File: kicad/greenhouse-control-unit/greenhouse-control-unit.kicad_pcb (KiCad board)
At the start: 2 copper layers, 55 parts, among them J1 Screw_Terminal_01x02, J10 Conn_01x15_Female, J10_LittleBuck1 Conn_01x01_Female, J11 Conn_01x02_Male, J11_LittleBuck1 Conn_01x01_Female, J12 Screw_Terminal_01x16, J12_BigBuck1 Conn_01x01_Female, J13 Conn_01x10_Female, J13_BigBuck1 Conn_01x01_Female, J14_LittleBuck1 Conn_01x01_Female, J15_LittleBuck1 Conn_01x01_Female, J2 Screw_Terminal_01x02, J3 Screw_Terminal_01x02, J4 Screw_Terminal_01x02, J5 Conn_01x02_Male, J6 Conn_01x03_Male, J6_BigBuck1 Conn_01x01_Female, J7 Conn_01x10_Female, J7_BigBuck1 Conn_01x01_Female, J8 Conn_01x10_Female, J9 Conn_01x15_Female, Q1 IRLB8721PBF, Q2 2N2222A, Q3 2N2222A, Q4 2N2222A, Q5 IRLB8721PBF, Q6 IRLB8721PBF, Q7 IRLB8721PBF, Q8 IRLB8721PBF, U1 74HC595, U2 74HC595

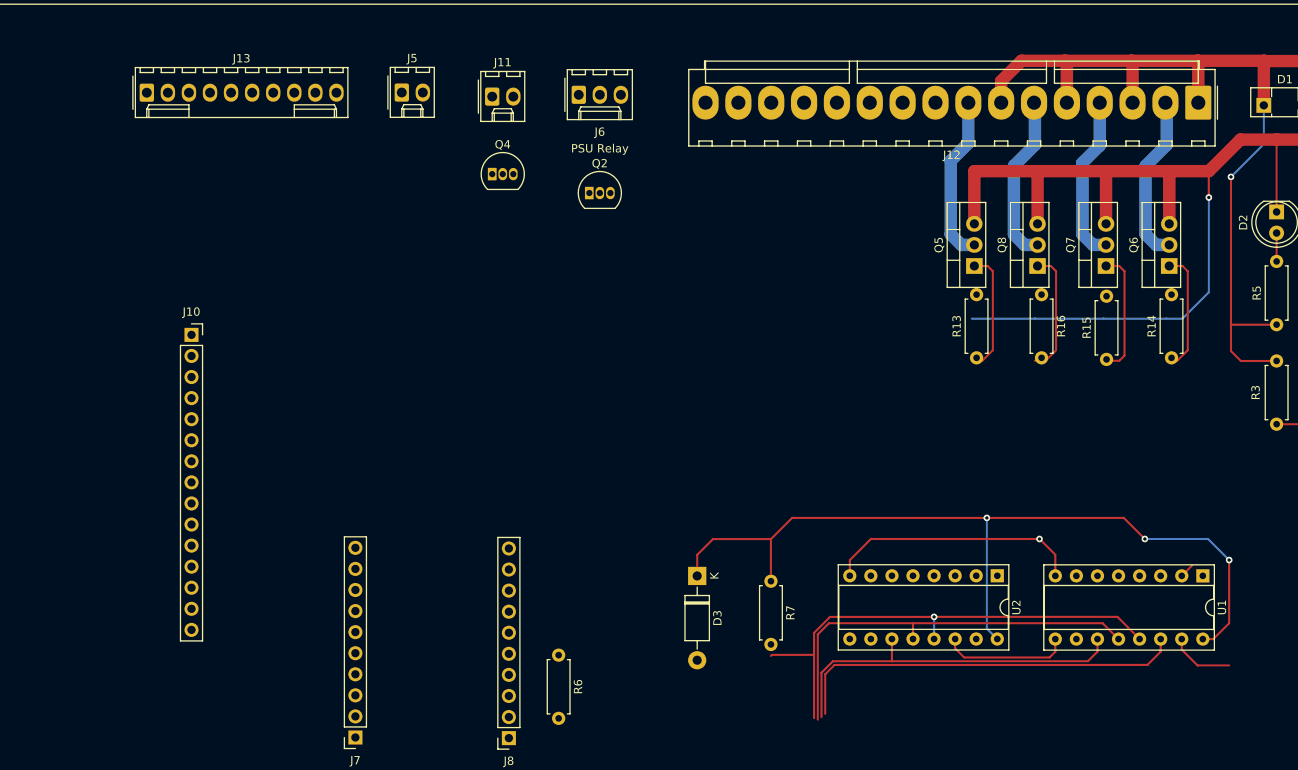
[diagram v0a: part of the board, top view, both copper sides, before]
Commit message: R values, rearrange SRs on PCB
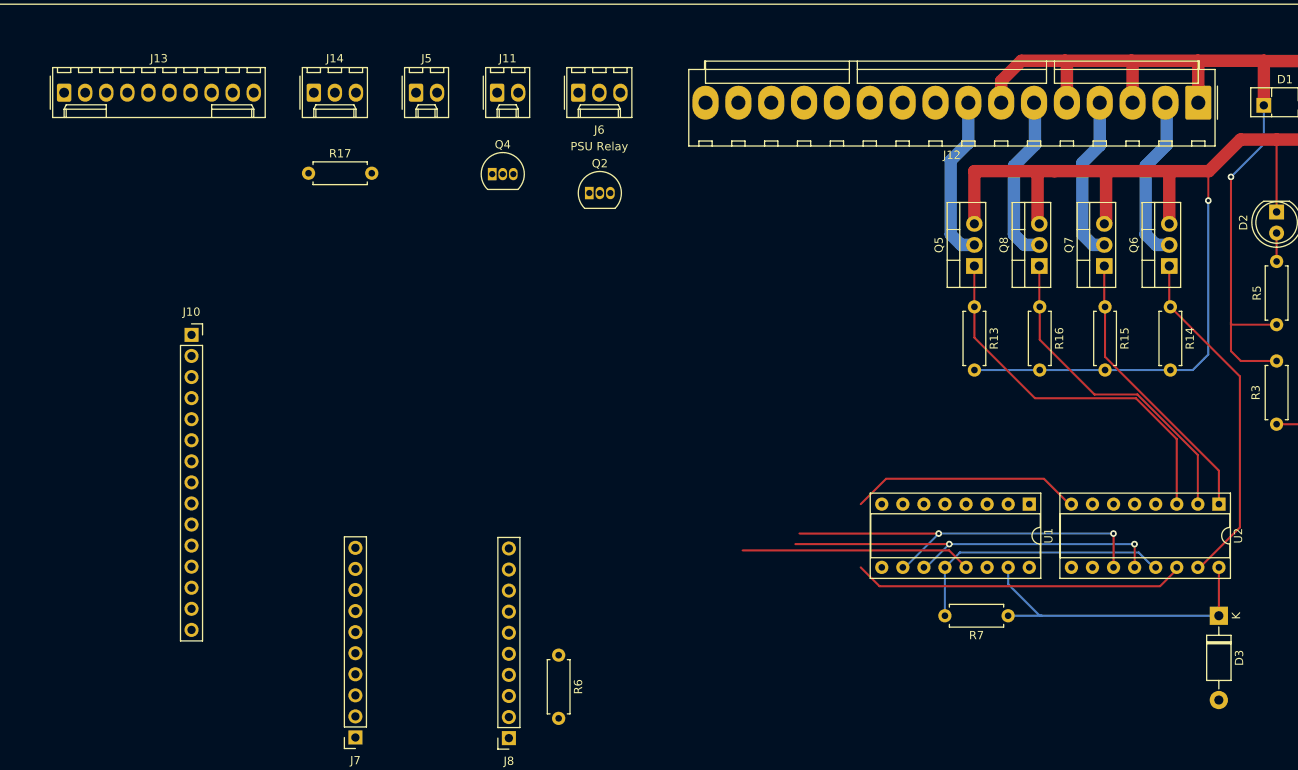
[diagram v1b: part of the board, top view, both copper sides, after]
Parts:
- added J14: Conn_01x03_Male, Connector_Molex:Molex_KK-254_AE-6410-03A_1x03_P2.54mm_Vertical, F.Cu at (83.9, 39.1)
- added R17: 4k6, Resistor_THT:R_Axial_DIN0207_L6.3mm_D2.5mm_P7.62mm_Horizontal, F.Cu at (83.3, 48.8)
- D1: value D_Schottky -> DSB20I15PA Schottky
- R1, R3: value 5k -> 4k6
- R10: value R4k6 -> 4k6
- R13, R14, R15, R16, R7, R9: value R10k -> 10k
- R2, R4: value 10k -> 1k
- moved D3 63.1 mm to (193.0, 102.1)
- moved R7 28.9 mm to (167.6, 102.1), turned to 180 degrees
- moved U2 28.1 mm to (193.1, 88.7)
- moved U1 22.6 mm to (170.2, 88.7)
- moved J13 9.97 mm to (53.8, 39.1)
- moved R15 6.34 mm to (179.3, 64.9), turned to -90 degrees
- moved R13 6.15 mm to (163.6, 64.9), turned to -90 degrees
- moved R14 6.15 mm to (187.2, 64.9), turned to -90 degrees
- moved J5 1.72 mm to (96.3, 39.1)
- moved R16 1.49 mm to (171.4, 64.9)
- moved J11 0.76 mm to (106.0, 39.1)
- moved J6 0.26 mm to (115.8, 39.1)
- moved Q7 0.21 mm to (179.2, 59.9)
- moved Q8 0.21 mm to (171.4, 59.9)
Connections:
- J13 pad 1: +5VA -> +3V3
- J13 pad 2: +3V3 -> GND
- J13 pad 3: GND -> unconnected-(J13-Pad3)
- J4 pad 2: GND -> +12V
- U1 pad 6: /SR_Q6 -> /Motor_IN1
- U1 pad 7: /SR_Q7 -> /Motor_IN2
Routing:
- net /SR_VCC: track 102.4 -> 38.7 mm, vias 3 -> 0
- net /MC_D6: track 47.9 -> 0.00 mm
- net /SW3_SR_Q10: track 0.00 -> 40.1 mm
- net /SW4_SR_Q11: track 15.1 -> 46.2 mm
- net /SW1_SR_Q08: track 15.1 -> 42.2 mm
- net Net-(U1-Pad9): track 15.5 -> 39.9 mm
- net /SW2_SR_Q09: track 15.5 -> 35.1 mm
- net GND: track 321.8 -> 309.9 mm, vias 2 -> 1
- net /BattRelayNC_SR_Q0: track 24.8 -> 17.1 mm
- net /MC_D7: track 43.9 -> 48.3 mm, vias 0 -> 2
- net /CaseFan_SR_Q2: track 1.80 -> 0.00 mm
- net /MC_D5: track 49.8 -> 48.3 mm, vias 0 -> 2
- net /MC_D0: track 61.4 -> 60.3 mm, vias 1 -> 0

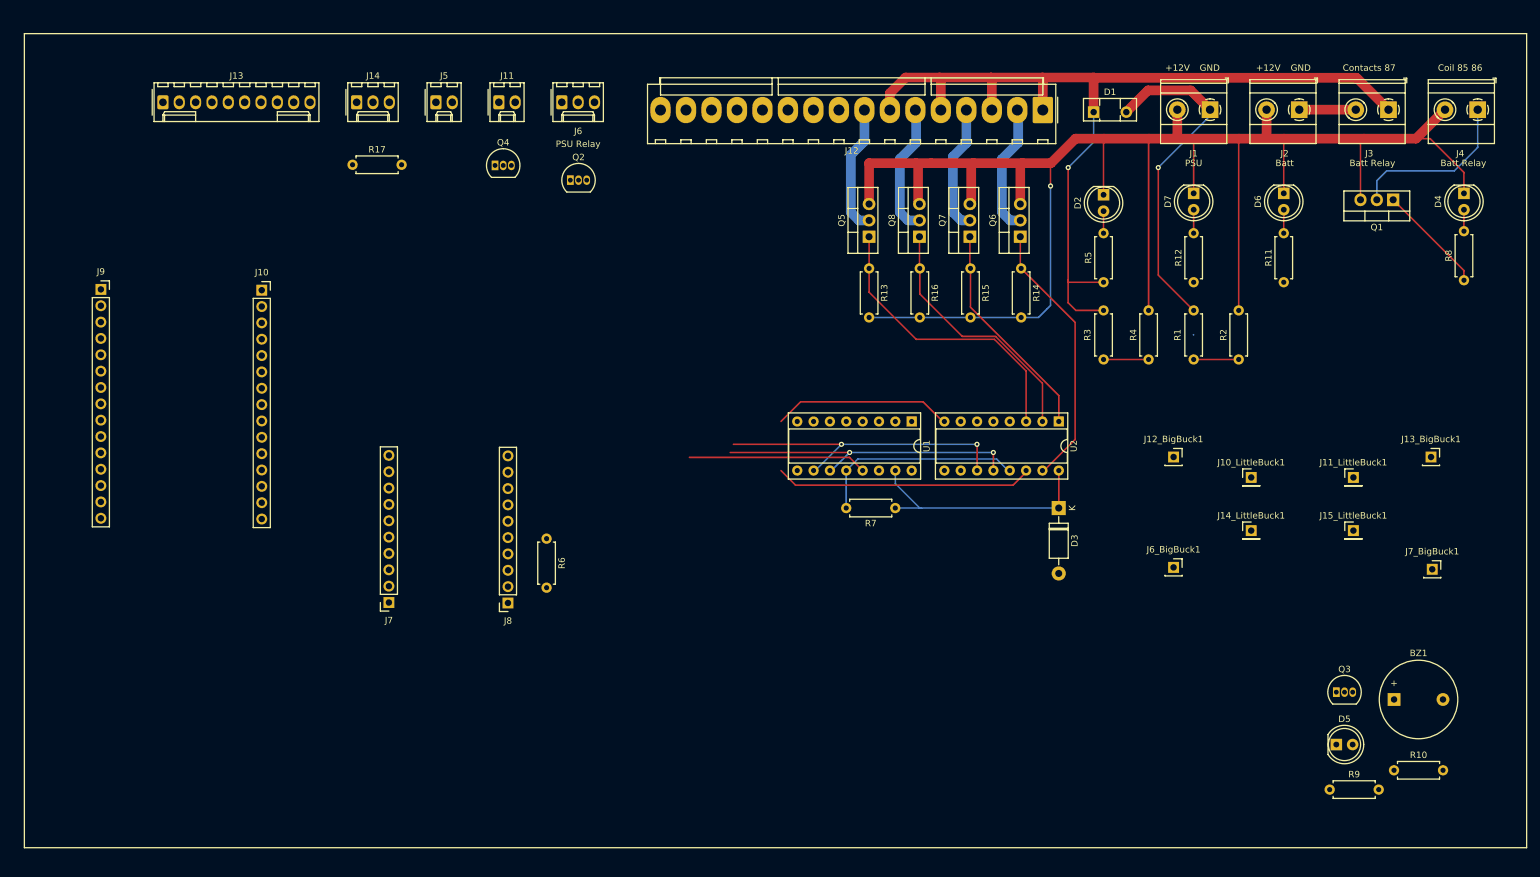
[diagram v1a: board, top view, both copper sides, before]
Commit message: Replaced BJTs with FETs, used horizontal FETs
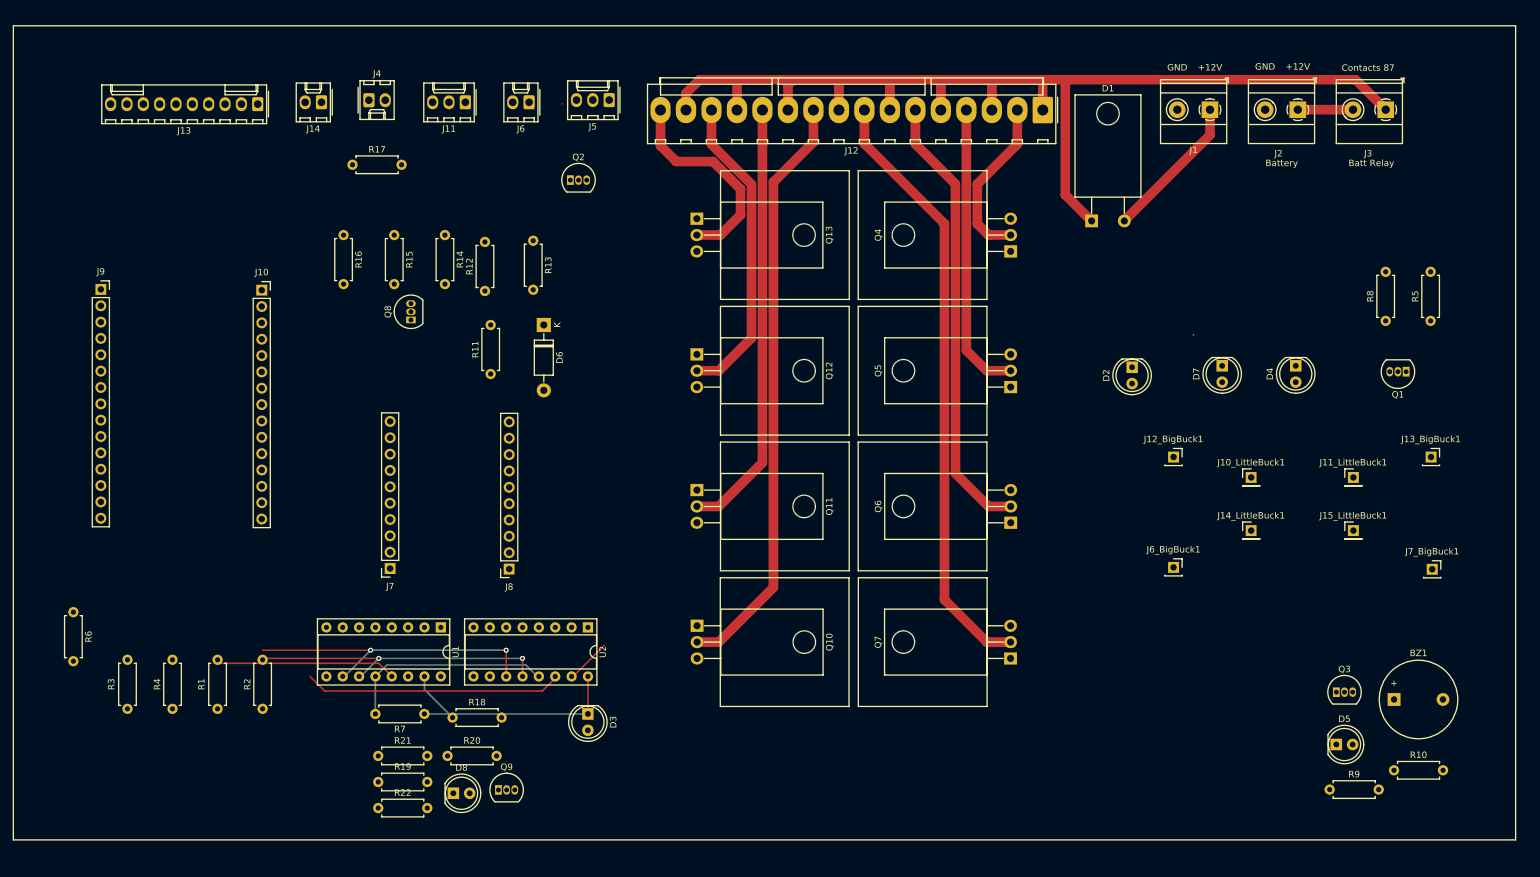
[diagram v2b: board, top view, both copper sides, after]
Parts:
- removed the J5 at (96.3, 39.1)
- added D8: LED, LED_THT:LED_D5.0mm, F.Cu at (99.0, 146.4)
- added J4: Molex_KK-254_01x02, Connector_Molex:Molex_KK-254_AE-6410-02A_1x02_P2.54mm_Vertical, F.Cu at (85.9, 38.7)
- added Q10: IRLB8721PBF, Package_TO_SOT_THT:TO-220-3_Horizontal_TabDown, F.Cu at (136.8, 120.4)
- added Q11: IRLB8721PBF, Package_TO_SOT_THT:TO-220-3_Horizontal_TabDown, F.Cu at (136.8, 99.3)
- added Q12: IRLB8721PBF, Package_TO_SOT_THT:TO-220-3_Horizontal_TabDown, F.Cu at (136.8, 78.2)
- added Q13: IRLB8721PBF, Package_TO_SOT_THT:TO-220-3_Horizontal_TabDown, F.Cu at (136.8, 57.1)
- added Q9: 2N7000, Package_TO_SOT_THT:TO-92_Inline, F.Cu at (106.0, 145.9)
- added R18: 10k, Resistor_THT:R_Axial_DIN0207_L6.3mm_D2.5mm_P7.62mm_Horizontal, F.Cu at (98.9, 134.7)
- added R19: 10k, Resistor_THT:R_Axial_DIN0207_L6.3mm_D2.5mm_P7.62mm_Horizontal, F.Cu at (87.3, 144.7)
- added R20: 10k, Resistor_THT:R_Axial_DIN0207_L6.3mm_D2.5mm_P7.62mm_Horizontal, F.Cu at (98.1, 140.6)
- added R21: 10k, Resistor_THT:R_Axial_DIN0207_L6.3mm_D2.5mm_P7.62mm_Horizontal, F.Cu at (87.3, 140.6)
- added R22: 10k, Resistor_THT:R_Axial_DIN0207_L6.3mm_D2.5mm_P7.62mm_Horizontal, F.Cu at (87.3, 148.7)
- D1: footprint Package_TO_SOT_THT:TO-126-2_Vertical -> Package_TO_SOT_THT:TO-220-2_Horizontal_TabDown
- D3: value 1N4001 -> LED; footprint Diode_THT:D_DO-41_SOD81_P10.16mm_Horizontal -> LED_THT:LED_D5.0mm
- D6: value LED -> 1N4001; footprint LED_THT:LED_D5.0mm -> Diode_THT:D_DO-41_SOD81_P10.16mm_Horizontal
- J1: renamed from J2; value Screw_Terminal_01x02 -> Pluggable_Terminal_01x02
- J11: value Conn_01x02_Male -> Molex_KK-254_01x03; footprint Connector_Molex:Molex_KK-254_AE-6410-02A_1x02_P2.54mm_Vertical -> Connector_Molex:Molex_KK-254_AE-6410-03A_1x03_P2.54mm_Vertical
- J12: value Screw_Terminal_01x16 -> Molex_KK-396_01x16
- J13: value Conn_01x10_Female -> Molex_KK-254_01x10
- J14, J6: value Conn_01x03_Male -> Molex_KK-254_01x02; footprint Connector_Molex:Molex_KK-254_AE-6410-03A_1x03_P2.54mm_Vertical -> Connector_Molex:Molex_KK-254_AE-6410-02A_1x02_P2.54mm_Vertical
- J2: renamed from J3; value Screw_Terminal_01x02 -> Pluggable_Terminal_01x02
- J3: renamed from J4; value Screw_Terminal_01x02 -> Pluggable_Terminal_01x02
- J5: renamed from J1; value Screw_Terminal_01x02 -> Molex_KK-254_01x03; footprint TerminalBlock_Phoenix:TerminalBlock_Phoenix_MKDS-1,5-2-5.08_1x02_P5.08mm_Horizontal -> Connector_Molex:Molex_KK-254_AE-6410-03A_1x03_P2.54mm_Vertical
- Q1, Q8: value IRLB8721PBF -> 2N7000; footprint Package_TO_SOT_THT:TO-220-3_Vertical -> Package_TO_SOT_THT:TO-92_Inline
- Q2, Q3: value 2N2222A -> 2N7000
- Q4: value 2N2222A -> IRLB8721PBF; footprint Package_TO_SOT_THT:TO-92_Inline -> Package_TO_SOT_THT:TO-220-3_Horizontal_TabDown
- Q5, Q6, Q7: footprint Package_TO_SOT_THT:TO-220-3_Vertical -> Package_TO_SOT_THT:TO-220-3_Horizontal_TabDown
- R11: value 2k -> 1k
- R12, R8: value 2k -> 10k
- R13, R14: value 10k -> 1k
- R17: value 4k6 -> 10k
- R6, R7, R9: value 10k -> 2k
- moved R1 161.1 mm to (62.3, 125.7)
- moved R2 161.1 mm to (69.3, 133.3)
- moved R3 161.1 mm to (48.3, 125.7)
- moved R4 161.1 mm to (55.3, 133.3)
- moved R11 124.1 mm to (104.8, 81.3)
- moved D6 116.8 mm to (113.0, 73.7)
- moved R12 110.1 mm to (103.9, 68.4)
- moved J5 93.4 mm to (123.2, 38.7)
- moved R14 89.7 mm to (97.7, 59.7)
- moved R15 89.7 mm to (89.8, 59.7)
- moved R16 89.7 mm to (81.9, 59.7)
- moved Q4 81.2 mm to (185.6, 62.2), turned to 90 degrees
- moved Q8 80.1 mm to (92.4, 72.9)
- moved U2 79.9 mm to (119.9, 120.7)
- moved D3 79.9 mm to (119.9, 134.1)
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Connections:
- BZ1 pad 1: Net-(BZ1-Pad1) -> +5V
- BZ1 pad 2: GND -> Net-(BZ1-Pad2)
- D3 pad 1: /SR_VCC -> /BattRelayNC_Coil
- D3 pad 2: +5VA -> Net-(D3-Pad2)
- D4 pad 1: GND -> Net-(D4-Pad1)
- D5 pad 2: Net-(BZ1-Pad1) -> +5V
- D6 pad 1: GND -> /SR_VCC
- D6 pad 2: Net-(D6-Pad2) -> +5VA
- J1 pad 1: /Batt+12V -> /PSU+12V
- J11 pad 1: Net-(J11-Pad1) -> +5V
- J11 pad 2: GND -> /Motor_IN1
- J12 pad 10: unconnected-(J12-Pad10) -> /SW_FET4
- J12 pad 11: unconnected-(J12-Pad11) -> +12V
- J12 pad 12: unconnected-(J12-Pad12) -> /SW_FET5
- J12 pad 13: unconnected-(J12-Pad13) -> +12V
- J12 pad 14: unconnected-(J12-Pad14) -> /SW_FET6
- J12 pad 15: unconnected-(J12-Pad15) -> +12V
- J12 pad 16: unconnected-(J12-Pad16) -> /SW_FET7
- J12 pad 2: /SW_FET1 -> /SW_FET0
- J12 pad 4: /SW_FET2 -> /SW_FET1
- J12 pad 6: /SW_FET3 -> /SW_FET2
- J12 pad 8: /SW_FET4 -> /SW_FET3
- J12 pad 9: unconnected-(J12-Pad9) -> +12V
- J14 pad 1: +3V3 -> +12V
- J14 pad 2: /Motor_IN1 -> GND
- J2 pad 1: +12V -> /Batt+12V
- J2 pad 2: /Batt+12V -> GND
- J3 pad 1: /BattRelayNC_Coil -> +12V
- J3 pad 2: +12V -> /Batt+12V
- J5 pad 1: /PSU+12V -> +12V
- J6 pad 1: +12V -> +5V
- J6 pad 2: /PsuRelayNC_GND -> Net-(D4-Pad1)
- Q1 pad 1: /BattRelayNC_SR_Q0 -> GND
- Q1 pad 2: /BattRelayNC_Coil -> /BattRelayNC_SR_Q0
- Q1 pad 3: GND -> /BattRelayNC_Coil
- Q2 pad 1: /PsuRelayNC_Coil -> GND
- Q2 pad 2: /PsuRelayNC_SR_Q3 -> /CaseFan_SR_Q2
- Q2 pad 3: +5V -> Net-(D4-Pad1)
- Q3 pad 1: Net-(BZ1-Pad1) -> GND
- Q3 pad 3: +5V -> Net-(Q3-Pad3)
- Q4 pad 1: Net-(J11-Pad1) -> /SW0_SR_Q08
- Q4 pad 2: /CaseFan_SR_Q2 -> /SW_FET0
- Q4 pad 3: +5V -> GND
- Q5 pad 1: /SW4_SR_Q11 -> /SW1_SR_Q09
- Q5 pad 2: /SW_FET4 -> /SW_FET1
- Q6 pad 1: /SW1_SR_Q08 -> /SW2_SR_Q10
- Q6 pad 2: /SW_FET1 -> /SW_FET2
- Q7 pad 1: /SW2_SR_Q09 -> /SW3_SR_Q11
- Q7 pad 2: /SW_FET2 -> /SW_FET3
- Q8 pad 1: /SW3_SR_Q10 -> /Motor_IN2
- Q8 pad 2: /SW_FET3 -> /SR_Q7
- Q8 pad 3: GND -> +5V
- R10 pad 1: Net-(D5-Pad1) -> +3V3
- R10 pad 2: GND -> /MC_D3
- R11 pad 1: /BatteryLed_SR_Q4 -> Net-(BZ1-Pad2)
- R11 pad 2: Net-(D6-Pad2) -> Net-(Q3-Pad3)
- R12 pad 1: /PsuLed_SR_Q5 -> /SR_VCC
- R12 pad 2: Net-(D7-Pad2) -> /MC_D0
- R13 pad 1: /SW4_SR_Q11 -> /BatteryLed_SR_Q4
- R13 pad 2: GND -> Net-(D7-Pad2)
- R14 pad 1: /SW1_SR_Q08 -> /PsuLed_SR_Q5
- R14 pad 2: GND -> Net-(D8-Pad2)
- R15 pad 1: /SW2_SR_Q09 -> /SW0_SR_Q08
- R16 pad 1: /SW3_SR_Q10 -> /SW1_SR_Q09
- R17 pad 1: +3V3 -> /SW2_SR_Q10
- R17 pad 2: /MC_D3 -> GND
- R6 pad 1: /ADC2_ADDR -> +5V
- R6 pad 2: GND -> Net-(D3-Pad2)
- R7 pad 1: /SR_VCC -> +5V
- R7 pad 2: /MC_D0 -> Net-(D4-Pad2)
- R8 pad 1: /BattRelayNC_SR_Q0 -> /ADC2_ADDR
- R8 pad 2: Net-(D4-Pad2) -> GND
- R9 pad 1: GND -> Net-(D5-Pad1)
- R9 pad 2: /StartBeep_SR_Q1 -> Net-(Q3-Pad3)
- U1 pad 3: /PsuRelayNC_SR_Q3 -> /PsuRelayNC_Coil
- U1 pad 6: /Motor_IN1 -> /SR_Q6
- U1 pad 7: /Motor_IN2 -> /SR_Q7
- U2 pad 1: /SW2_SR_Q09 -> /SW1_SR_Q09
- U2 pad 15: /SW1_SR_Q08 -> /SW0_SR_Q08
- U2 pad 2: /SW3_SR_Q10 -> /SW2_SR_Q10
- U2 pad 3: /SW4_SR_Q11 -> /SW3_SR_Q11
- U2 pad 4: /SR_Q12 -> /SW4_SR_Q12
- U2 pad 5: /SR_Q13 -> /SW5_SR_Q13
- U2 pad 6: /SR_Q14 -> /SW6_SR_Q14
- U2 pad 7: /SR_Q15 -> /SW7_SR_Q15
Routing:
- net GND: track 309.9 -> 0.16 mm, vias 1 -> 0
- net /SW_FET3: track 20.4 -> 94.2 mm
- net /SW_FET4: track 20.1 -> 92.1 mm
- net /SW_FET5: track 0.00 -> 67.8 mm
- net /SW_FET2: track 20.1 -> 69.9 mm
- net /SW_FET6: track 0.00 -> 48.6 mm
- net unconnected-(U1-Pad10): track 0.00 -> 48.3 mm, vias 0 -> 2
- net /MC_D7: track 48.3 -> 0.00 mm, vias 2 -> 0
- net /SW4_SR_Q11: track 46.2 -> 0.00 mm
- net /SW1_SR_Q08: track 42.2 -> 0.00 mm
- net /SW3_SR_Q10: track 40.1 -> 0.00 mm
- net /SW2_SR_Q09: track 35.1 -> 0.00 mm
- net /SW_FET7: track 0.00 -> 32.9 mm
- net /MC_D0: track 60.3 -> 32.6 mm
- net /BattRelayNC_Coil: track 26.6 -> 0.00 mm
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
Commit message: Laid out PCB around new FET layout
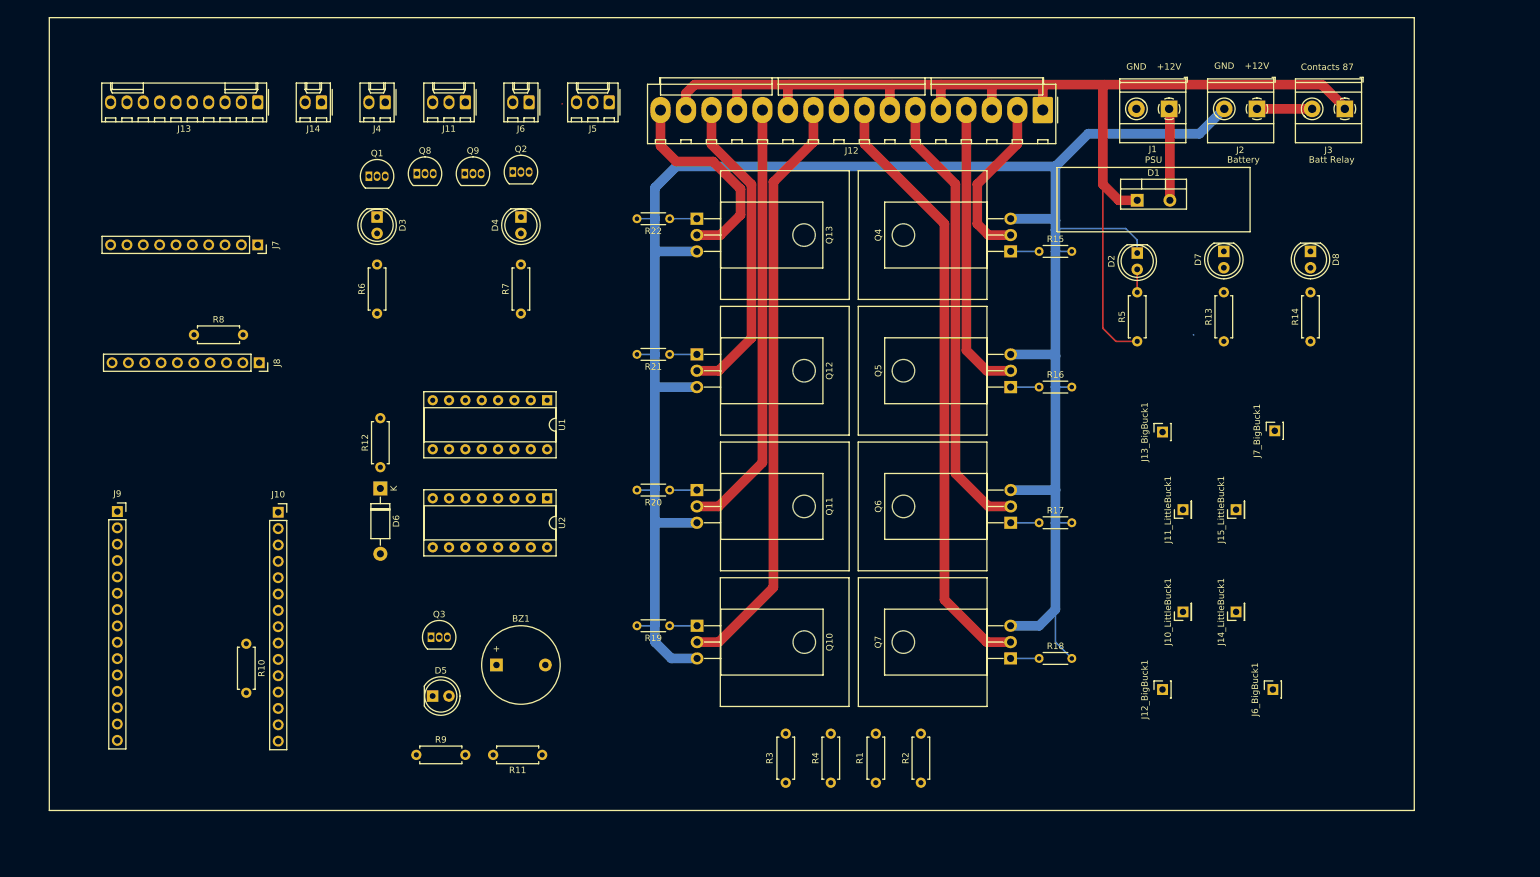
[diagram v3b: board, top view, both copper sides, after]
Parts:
- D1: footprint Package_TO_SOT_THT:TO-220-2_Horizontal_TabDown -> Package_TO_SOT_THT:TO-220-2_Vertical
- R15, R16, R17, R18, R19, R20, R21, R22: footprint Resistor_THT:R_Axial_DIN0207_L6.3mm_D2.5mm_P7.62mm_Horizontal -> Resistor_THT:R_Axial_DIN0204_L3.6mm_D1.6mm_P5.08mm_Horizontal
- moved R8 185.2 mm to (58.7, 75.2), turned to 0 degrees
- moved R10 179.4 mm to (66.8, 123.2), turned to -90 degrees
- moved Q1 164.0 mm to (85.9, 50.5), turned to 0 degrees
- moved D8 157.6 mm to (232.2, 62.2), turned to -90 degrees
- moved R9 142.0 mm to (93.2, 140.5)
- moved Q3 140.9 mm to (95.5, 122.2)
- moved D5 140.6 mm to (95.8, 131.3)
- moved BZ1 139.6 mm to (105.7, 126.5)
- moved R14 135.5 mm to (232.2, 76.2), turned to 90 degrees
- moved D4 122.6 mm to (109.5, 56.9)
- moved R17 120.3 mm to (190.0, 104.4)
- moved R16 110.6 mm to (190.0, 83.3), turned to 0 degrees
- moved R13 108.4 mm to (218.7, 76.2), turned to 90 degrees
- moved R1 102.9 mm to (164.6, 137.2)
- moved R2 102.9 mm to (171.6, 144.8)
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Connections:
- J4 pad 1: /BattRelayNC_Coil -> +12V
- J4 pad 2: +12V -> /BattRelayNC_Coil
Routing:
- net GND: track 0.16 -> 332.7 mm
- net unconnected-(U1-Pad10): track 48.3 -> 0.00 mm, vias 2 -> 0
- net /MC_D5: track 48.3 -> 0.00 mm, vias 2 -> 0
- net Net-(U1-Pad9): track 39.9 -> 0.00 mm
- net /SR_VCC: track 38.7 -> 0.00 mm
- net /PSU+12V: track 50.7 -> 14.3 mm
- net /MC_D0: track 32.6 -> 0.00 mm
- net +12V: track 171.6 -> 185.7 mm
- net /SW3_SR_Q11: track 0.00 -> 4.44 mm
- net /SW1_SR_Q09: track 0.00 -> 4.42 mm
- net /SW2_SR_Q10: track 0.00 -> 4.41 mm
- net /SW4_SR_Q12: track 0.00 -> 4.26 mm
- net /SW5_SR_Q13: track 0.00 -> 4.23 mm
- net /SW6_SR_Q14: track 0.00 -> 4.23 mm
- net /SW7_SR_Q15: track 0.00 -> 4.22 mm
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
